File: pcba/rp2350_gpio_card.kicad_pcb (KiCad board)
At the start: 2 copper layers, 26 x 30 mm, 11 parts, among them P1 USB_C_Plug_USB2.0, U1 AP2112K-3.3

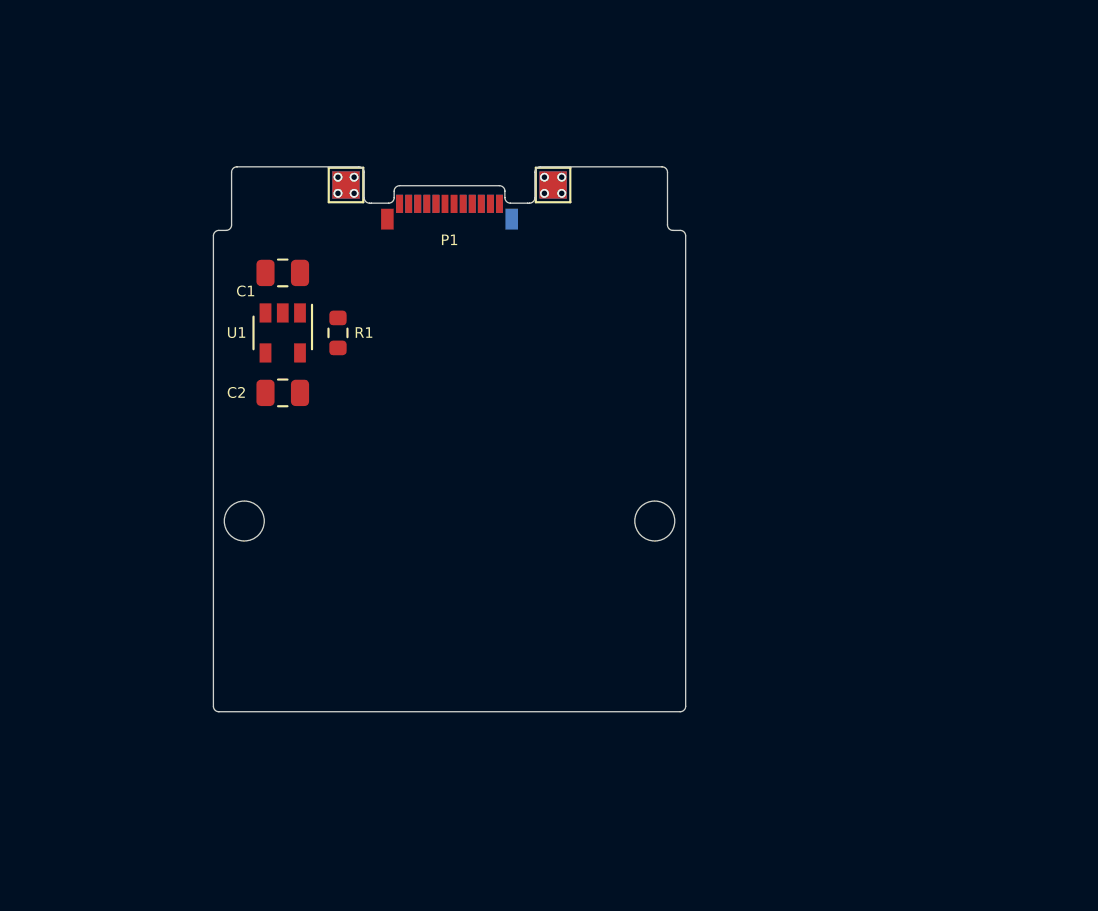
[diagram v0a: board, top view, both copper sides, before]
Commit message: update schematics and start working on pcb (very WIP, need help)
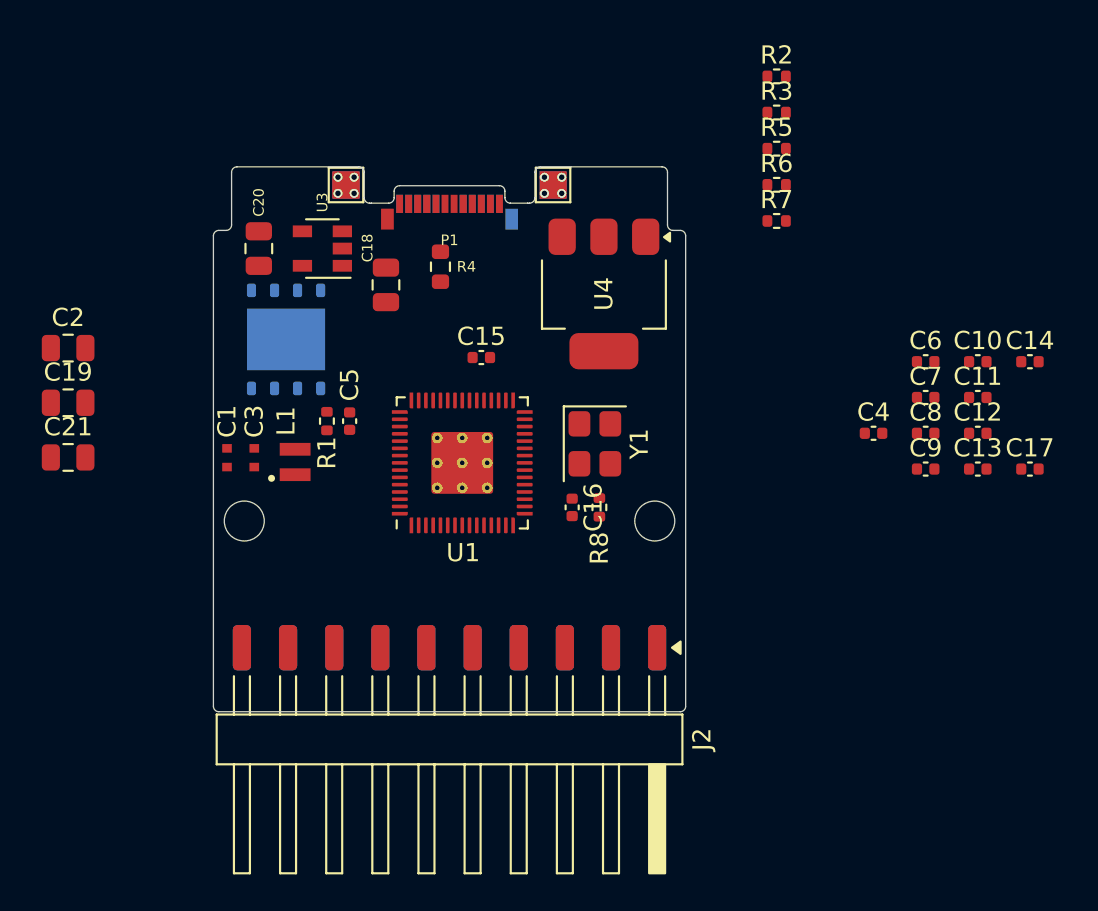
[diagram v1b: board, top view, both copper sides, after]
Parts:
- added C1: 4.7u, RP2350_60QFN_minimal:C_0402_1005Metric_small_pads, F.Cu at (127.8, 143.0)
- added C10: 100n, Capacitor_SMD:C_0402_1005Metric, F.Cu at (169.1, 137.7)
- added C11: 100n, Capacitor_SMD:C_0402_1005Metric, F.Cu at (169.1, 139.7)
- added C12: 100n, Capacitor_SMD:C_0402_1005Metric, F.Cu at (169.1, 141.7)
- added C13: 100n, Capacitor_SMD:C_0402_1005Metric, F.Cu at (169.1, 143.6)
- added C14: 100n, Capacitor_SMD:C_0402_1005Metric, F.Cu at (172.0, 137.7)
- added C15: 15p, Capacitor_SMD:C_0402_1005Metric, F.Cu at (141.8, 137.5)
- added C16: 15p, Capacitor_SMD:C_0402_1005Metric, F.Cu at (146.8, 145.8)
- added C17: 100n, Capacitor_SMD:C_0402_1005Metric, F.Cu at (172.0, 143.6)
- added C19: 10u, Capacitor_SMD:C_0805_2012Metric, F.Cu at (119.0, 140.0)
- added C2: 10u, Capacitor_SMD:C_0805_2012Metric, F.Cu at (119.0, 137.0)
- added C21: 10u, Capacitor_SMD:C_0805_2012Metric, F.Cu at (119.0, 143.0)
- added C3: 4.7u, RP2350_60QFN_minimal:C_0402_1005Metric_small_pads, F.Cu at (129.2, 143.0)
- added C4: 100n, Capacitor_SMD:C_0402_1005Metric, F.Cu at (163.3, 141.7)
- added C5: 4.7u, Capacitor_SMD:C_0402_1005Metric, F.Cu at (134.5, 141.0)
- added C6: 4.7u, Capacitor_SMD:C_0402_1005Metric, F.Cu at (166.2, 137.7)
- added C7: 100n, Capacitor_SMD:C_0402_1005Metric, F.Cu at (166.2, 139.7)
- added C8: 100n, Capacitor_SMD:C_0402_1005Metric, F.Cu at (166.2, 141.7)
- added C9: 100n, Capacitor_SMD:C_0402_1005Metric, F.Cu at (166.2, 143.6)
- added J1: Conn_01x10_Pin, Connector_Harwin:Harwin_M20-89010xx_1x10_P2.54mm_Horizontal, B.Cu at (140.0, 159.0)
- added J2: Conn_01x10_Pin, Connector_Harwin:Harwin_M20-89010xx_1x10_P2.54mm_Horizontal, F.Cu at (140.0, 159.0)
- added L1: 3.3u, RP2350_60QFN_minimal:L_pol_2016, F.Cu at (131.5, 143.2)
- added R1: 33, Resistor_SMD:R_0402_1005Metric, F.Cu at (133.2, 141.0)
- added R2: 27, Resistor_SMD:R_0402_1005Metric, F.Cu at (158.0, 122.0)
- added R3: 27, Resistor_SMD:R_0402_1005Metric, F.Cu at (158.0, 124.0)
- added R5: DNF, Resistor_SMD:R_0402_1005Metric, F.Cu at (158.0, 126.0)
- added R6: 0, Resistor_SMD:R_0402_1005Metric, F.Cu at (158.0, 128.0)
- added R7: DNF, Resistor_SMD:R_0402_1005Metric, F.Cu at (158.0, 130.0)
- added R8: 1k, Resistor_SMD:R_0402_1005Metric, F.Cu at (148.2, 145.8)
- added U1: RP2350_60QFN, RP2350_60QFN_minimal:RP2350-QFN-60-1EP_7x7_P0.4mm_EP3.4x3.4mm_ThermalVias, F.Cu at (140.7, 143.3)
- added U2: W25Q128JVS, Package_SON:WSON-8-1EP_6x5mm_P1.27mm_EP3.4x4.3mm, B.Cu at (131.0, 136.5)
- added U4: NCP1117-3.3_SOT223, Package_TO_SOT_SMD:SOT-223-3_TabPin2, F.Cu at (148.5, 134.0)
- added Y1: ABM8-272-T3, Crystal:Crystal_SMD_3225-4Pin_3.2x2.5mm, F.Cu at (148.0, 142.2)
- moved C20 8.05 mm to (129.5, 131.5), turned to 90 degrees
- moved R4 6.72 mm to (139.5, 132.5)
- moved C18 5.72 mm to (136.5, 133.5), turned to 90 degrees
- moved U3 5.13 mm to (133.0, 131.5), turned to 180 degrees
- renumbered C1 to C18, C2 to C20, R1 to R4, TP3 to TP2, TP2 to TP3, U1 to U3
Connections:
- C18 pad 2: GND -> +3V3
- C20 pad 1: +3V3 -> +3.3V
- C20 pad 2: GND -> +3V3
- P1 pad A1: GND -> +3V3
- P1 pad A12: GND -> +3V3
- P1 pad A6: (no net) -> /USB_D+
- P1 pad A7: (no net) -> /USB_D-
- P1 pad B1: GND -> +3V3
- P1 pad B12: GND -> +3V3
- P1 pad B5: (no net) -> unconnected-(P1-VCONN-PadB5)
- P1 pad S1: GND -> +3V3
- R4 pad 2: GND -> +3V3
- TP1 pad 1: GND -> +3V3
- TP2 pad 1: GND -> +3V3
- TP3 pad 1: GND -> +3V3
- TP4 pad 1: GND -> +3V3
- U3 pad 2: GND -> +3V3
- U3 pad 4: (no net) -> unconnected-(U3-NC-Pad4)
- U3 pad 5: +3V3 -> +3.3V
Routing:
- net GND: vias 8 -> 0
- net +3V3: vias 0 -> 8
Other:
- net class Default removed

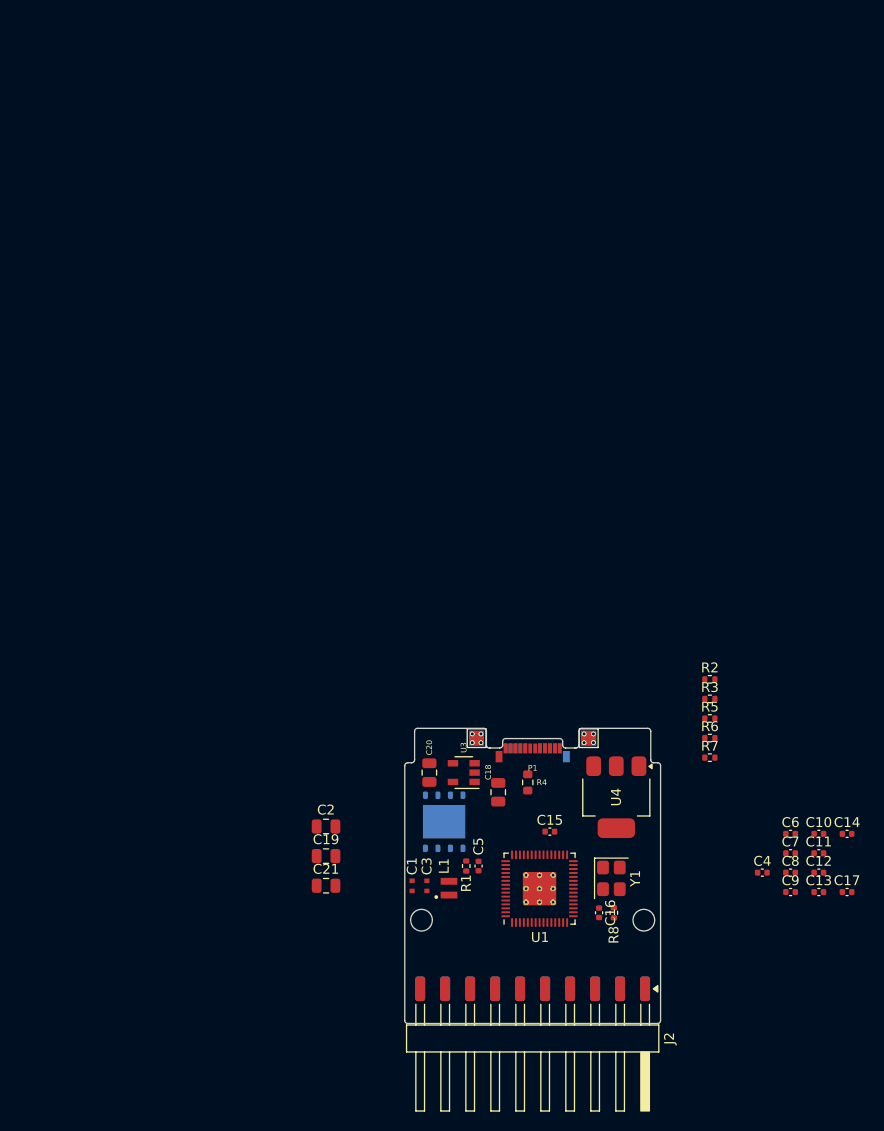
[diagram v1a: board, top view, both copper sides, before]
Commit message: finish first PCB prototype, modify schematic
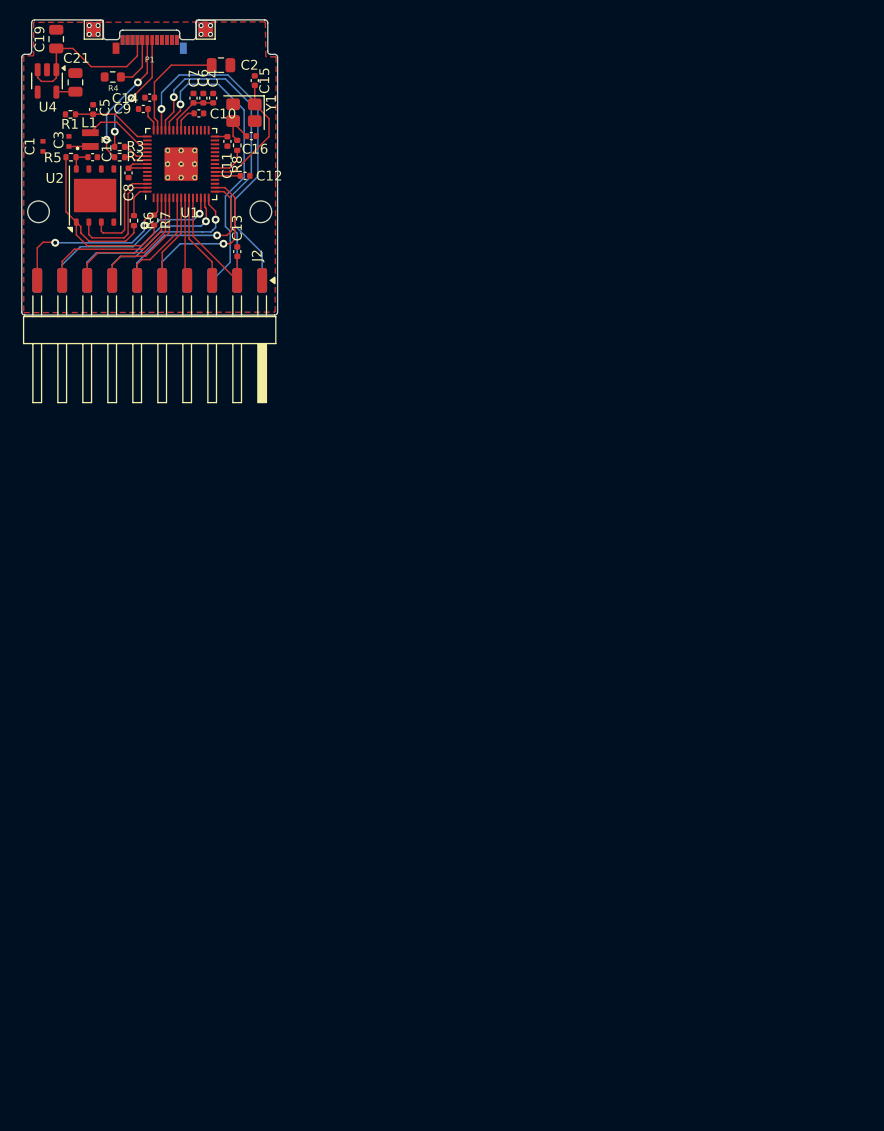
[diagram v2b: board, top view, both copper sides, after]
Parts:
- removed C18, C20: 10uF, Capacitor_SMD:C_0805_2012Metric
- removed U3: AP2112K-3.3, Package_TO_SOT_SMD:SOT-23-5
- U2: moved to F.Cu
- U4: value NCP1117-3.3_SOT223 -> AP2127K-3.3; footprint Package_TO_SOT_SMD:SOT-223-3_TabPin2 -> Package_TO_SOT_SMD:SOT-23-5
- moved C17 107.0 mm to (95.3, 69.0)
- moved C9 103.3 mm to (100.4, 64.0), turned to 180 degrees
- moved C14 103.1 mm to (101.1, 62.9), turned to 180 degrees
- moved C8 97.9 mm to (98.9, 70.5), turned to -90 degrees
- moved C7 97.8 mm to (105.5, 63.0), turned to 90 degrees
- moved C10 96.6 mm to (106.1, 64.5)
- moved C4 96.5 mm to (107.5, 63.0), turned to 90 degrees
- moved C6 95.7 mm to (106.5, 63.0), turned to 90 degrees
- moved C11 94.1 mm to (109.0, 67.3), turned to -90 degrees
- moved U4 93.0 mm to (90.6, 61.2)
- moved C12 91.7 mm to (110.8, 70.8)
- moved C13 87.9 mm to (110.0, 78.5), turned to 90 degrees
- moved C19 87.5 mm to (91.6, 57.0), turned to 90 degrees
- moved R8 86.9 mm to (110.0, 67.8)
- moved C16 86.5 mm to (111.4, 66.8), turned to 0 degrees
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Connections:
- C1 pad 1: +3V3 -> +3.3V
- C1 pad 2: +3V3 -> GND
- C10 pad 1: +3V3 -> +3.3V
- C10 pad 2: +3V3 -> GND
- C11 pad 1: +3V3 -> +3.3V
- C11 pad 2: +3V3 -> GND
- C12 pad 1: +3V3 -> +3.3V
- C12 pad 2: +3V3 -> GND
- C13 pad 1: +3V3 -> +3.3V
- C13 pad 2: +3V3 -> GND
- C14 pad 1: +3V3 -> +3.3V
- C14 pad 2: +3V3 -> GND
- C15 pad 2: +3V3 -> GND
- C16 pad 2: +3V3 -> GND
- C17 pad 1: +3V3 -> +3.3V
- C17 pad 2: +3V3 -> GND
- C19 pad 2: +3V3 -> GND
- C2 pad 1: +3V3 -> +3.3V
- C2 pad 2: +3V3 -> GND
- C21 pad 1: +3V3 -> +3.3V
- C21 pad 2: +3V3 -> GND
- C3 pad 2: +3V3 -> GND
- C4 pad 2: +3V3 -> GND
- C5 pad 2: +3V3 -> GND
- C6 pad 2: +3V3 -> GND
- C7 pad 2: +3V3 -> GND
- C8 pad 1: +3V3 -> +3.3V
- C8 pad 2: +3V3 -> GND
- C9 pad 1: +3V3 -> +3.3V
- C9 pad 2: +3V3 -> GND
- J1 pad 1: /RUN -> /GPIO8
- J1 pad 2: /QSPI_SS -> /GPIO9
- J1 pad 3: /GPIO8 -> /GPIO10
- J1 pad 4: /GPIO9 -> /GPIO11
- J1 pad 5: /GPIO10 -> /GPIO12
- J1 pad 6: /GPIO11 -> /GPIO13
- J2 pad 1: +3V3 -> GND
- J2 pad 10: /GPIO7 -> /GPIO0
- J2 pad 2: +3V3 -> +3.3V
- J2 pad 3: /GPIO0 -> /GPIO7
- J2 pad 4: /GPIO1 -> /GPIO6
- J2 pad 5: /GPIO2 -> /GPIO5
- J2 pad 6: /GPIO3 -> /GPIO4
- J2 pad 7: /GPIO4 -> /GPIO3
- J2 pad 8: /GPIO5 -> /GPIO2
- J2 pad 9: /GPIO6 -> /GPIO1
- P1 pad A1: +3V3 -> GND
- P1 pad A12: +3V3 -> GND
- P1 pad B1: +3V3 -> GND
- P1 pad B12: +3V3 -> GND
- P1 pad S1: +3V3 -> GND
- R1 pad 1: +3V3 -> +3.3V
- R4 pad 2: +3V3 -> GND
- R5 pad 1: +3V3 -> +3.3V
- TP1 pad 1: +3V3 -> GND
- TP2 pad 1: +3V3 -> GND
- TP3 pad 1: +3V3 -> GND
- TP4 pad 1: +3V3 -> GND
- U1 pad 1: +3V3 -> +3.3V
- U1 pad 11: +3V3 -> +3.3V
- U1 pad 20: +3V3 -> +3.3V
- U1 pad 30: +3V3 -> +3.3V
- U1 pad 38: +3V3 -> +3.3V
- U1 pad 44: +3V3 -> +3.3V
- U1 pad 45: +3V3 -> +3.3V
- U1 pad 47: +3V3 -> GND
- U1 pad 49: +3V3 -> +3.3V
- U1 pad 53: +3V3 -> +3.3V
- U1 pad 54: +3V3 -> +3.3V
- U1 pad 61: +3V3 -> GND
- U2 pad 4: +3V3 -> GND
- U2 pad 8: +3V3 -> +3.3V
- U2 pad 9: +3V3 -> GND
- U4 pad 1: +3V3 -> VBUS
- U4 pad 2: +3V3 -> GND
- Y1 pad 2: +3V3 -> GND
- Y1 pad 4: +3V3 -> GND
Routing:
- net +3.3V: track 0.00 -> 43.4 mm
- net /GPIO29_ADC3: track 0.00 -> 35.6 mm, vias 0 -> 1
- net /GPIO28_ADC2: track 0.00 -> 32.9 mm, vias 0 -> 1
- net /GPIO27_ADC1: track 0.00 -> 31.3 mm, vias 0 -> 1
- net /FLASH_SS: track 0.00 -> 26.2 mm
- net /GPIO9: track 0.00 -> 19.4 mm, vias 0 -> 1
- net /GPIO0: track 0.00 -> 19.1 mm, vias 0 -> 2
- net /GPIO10: track 0.00 -> 18.1 mm, vias 0 -> 1
- net /GPIO12: track 0.00 -> 18.0 mm, vias 0 -> 1
- net VBUS: track 0.00 -> 17.1 mm
- net /GPIO11: track 0.00 -> 17.0 mm, vias 0 -> 1
- net /GPIO13: track 0.00 -> 16.9 mm, vias 0 -> 1
- net /GPIO1: track 0.00 -> 16.6 mm
- net /GPIO2: track 0.00 -> 14.4 mm
- net /USB_D+: track 0.00 -> 14.0 mm, vias 0 -> 2
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- added copper zone on F.Cu, net GND

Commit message: update fillings
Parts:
- added REF**: OSHW-Logo2_7.3x6mm_SilkScreen, Symbol:OSHW-Logo2_7.3x6mm_SilkScreen, B.Cu at (95.2, 76.8)
- moved R4 0.41 mm to (97.2, 60.4)
- moved C15 0.27 mm to (111.8, 60.9)
- moved C8 0.17 mm to (98.8, 70.5)
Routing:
- net GND: track 0.00 -> 54.9 mm, vias 8 -> 16
- net VBUS: track 17.1 -> 16.3 mm
- added copper zone on F.Cu, net +3.3V
- added copper zone on B.Cu, net GND
- removed copper zone on F.Cu, net GND
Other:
- board text added: "Designer: Tan Siret Akıncı"
- board text added: "License: CC BY 4.0"

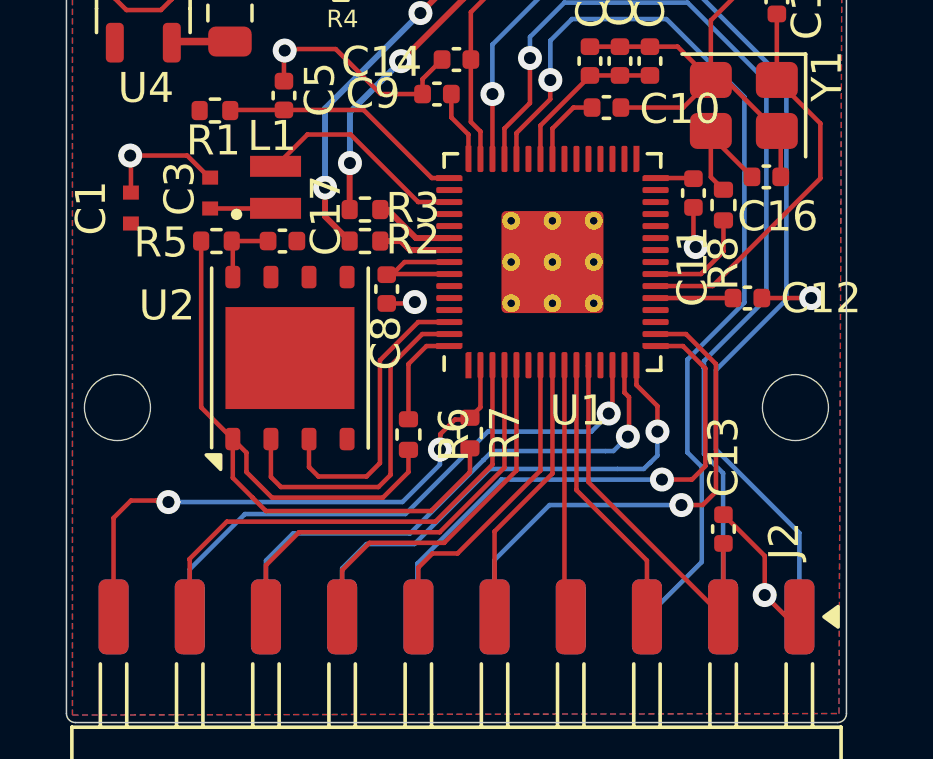
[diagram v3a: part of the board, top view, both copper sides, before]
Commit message: add silkscreen logos and stuff
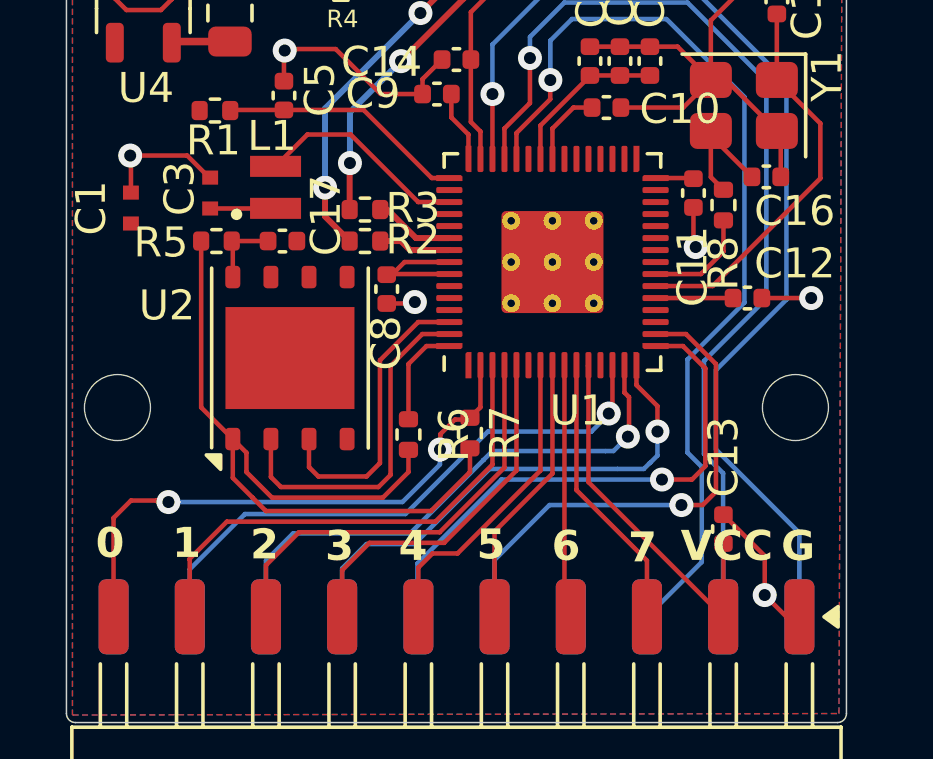
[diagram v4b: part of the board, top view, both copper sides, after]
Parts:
- moved REF** 15.8 mm to (109.7, 70.2)
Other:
- board text added: "0"
- board text added: "1"
- board text added: "10"
- board text added: "11"
- board text added: "12"
- board text added: "13"
- board text added: "2"
- board text added: "26"
- board text added: "27"
- board text added: "28"
- board text added: "29"
- board text added: "3"
- board text added: "4"
- board text added: "5"
- board text added: "6"
- board text added: "7"
- board text added: "8"
- board text added: "9"
- board text added: "G"
- board text added: "VCC"
- board text added: "{dblquote}Yes, it's pink{dblquote}"

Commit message: minor changes
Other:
- board text removed: "{dblquote}Yes, it's pink{dblquote}"
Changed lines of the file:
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@@
-		)
-	)
-	(gr_text "{dblquote}Yes, it's pink{dblquote}"
-		(at 104.4 59.75 0)
-		(layer "B.SilkS")
-		(effects
-			(font
-				(size 0.5842 0.5842)
-				(thickness 0.1016)
-				(bold yes)
-			)
-			(justify left bottom mirror)
 		)
 	)
